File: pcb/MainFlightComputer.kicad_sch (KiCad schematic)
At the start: 73 parts, among them J1 614105150721, J3 Micro_SD_Card, J4 Pinout, J5 Debug, SW1 B3U-1000P-B, SW2 B3U-1000P-B, U1 STM32H533VET6, U2 MCP2221A-I/ST, U3 AP2112K-3.3

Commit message: Placed down most of the components.
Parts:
- removed JP4: SolderJumper_2_Open, Jumper:SolderJumper-2_P1.3mm_Open_RoundedPad1.0x1.5mm, symbol Jumper:SolderJumper_2_Open
- added R32: 100, Resistor_SMD:R_1206_3216Metric_Pad1.30x1.75mm_HandSolder, symbol Device:R
- SW1, SW2: value B3U-1000P-B -> B3U-1000P; footprint Button_Switch_SMD:SW_SPST_B3U-1000P-B -> Button_Switch_SMD:SW_SPST_B3U-1000P
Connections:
- net +3.3V: now also R32.1
- net RESET: now also R32.2
- net VBUS_VIN_LED_ANODE: now reaches D5.2 (A), R15.2
- net RESET_PRESSED: now reaches R16.1, SW1.2
- net BUTTON_PRESSED: now reaches R18.1, SW2.2
- net VBUS_VOUT_LED_ANODE: now reaches D3.2 (A), R14.2
- net BOOT0_VALUE: now reaches JP1.2 (C), R17.1
- net DEBUG_LED_G_CATHODE: now reaches D4.4 (GK), R12.1
- net DEBUG_LED_B_CATHODE: now reaches D4.2 (BK), R13.1
- net DEBUG_LED_R_CATHODE: now reaches D4.3 (RK), R11.1
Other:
- note added: "Debug LED (V2 : Added net-labels)."
- note added: "Reset Mechanism (V3 : Pull-up footprint)."
- note added: "USB-UART Bridge (V5 : Added more net-labels)."
- note removed: "Debug LED (V1 : Lowercase nets)."
- note removed: "Reset Mechanism."
- note removed: "USB-UART Bridge (V4 : Added net-labels)."
- moved on the sheet: C11, D3, D5, R11, R13, R16, R17, R18, SW1

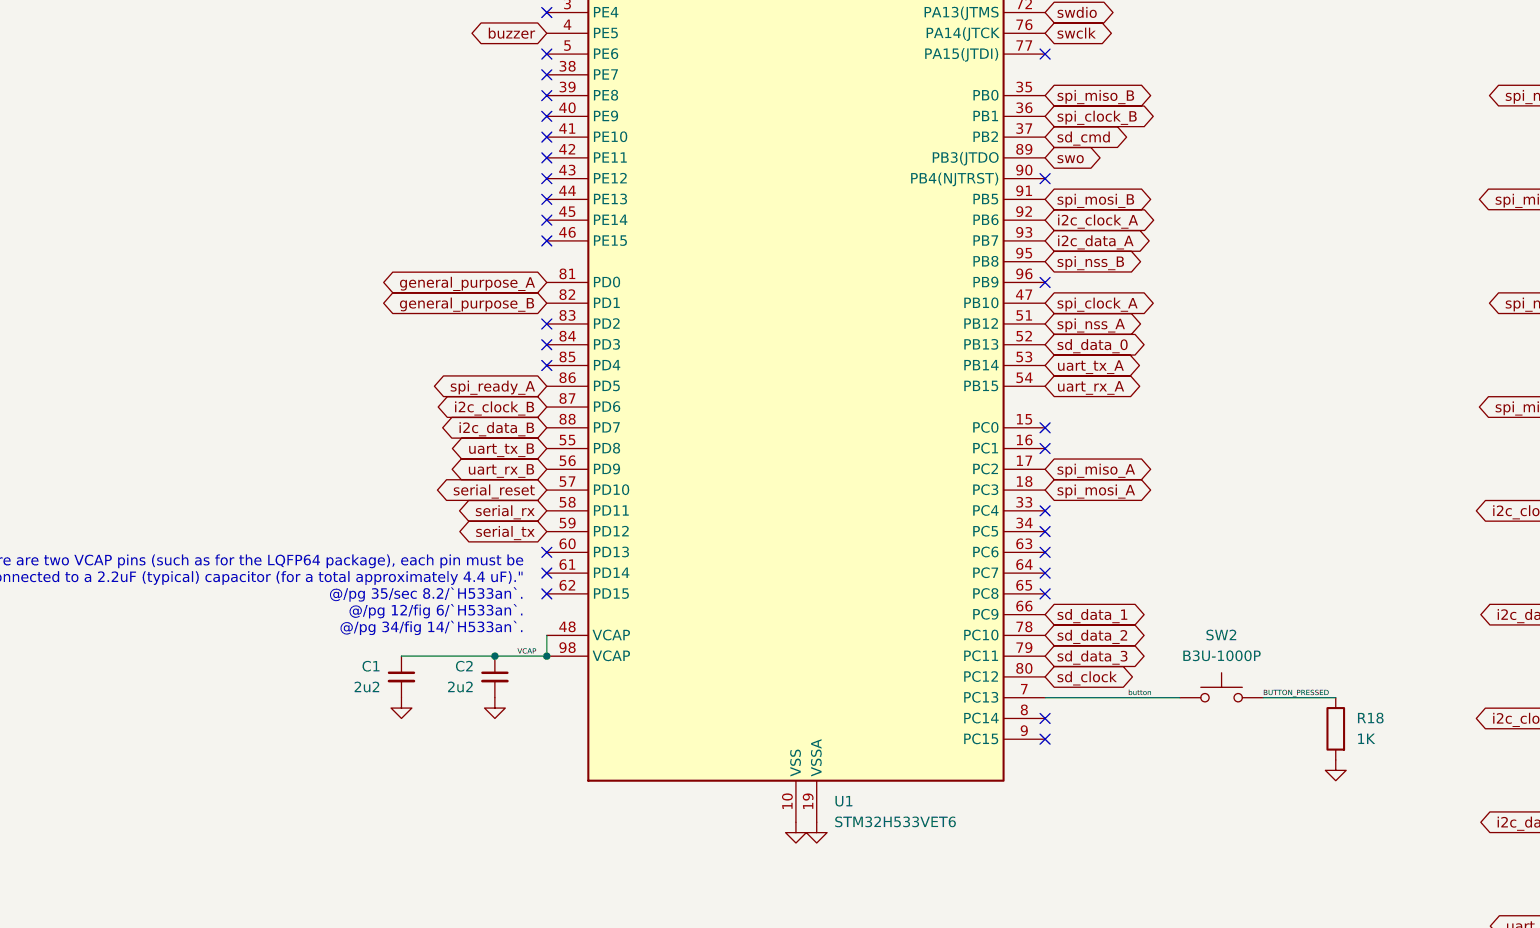
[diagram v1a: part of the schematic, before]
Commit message: Routed user button.
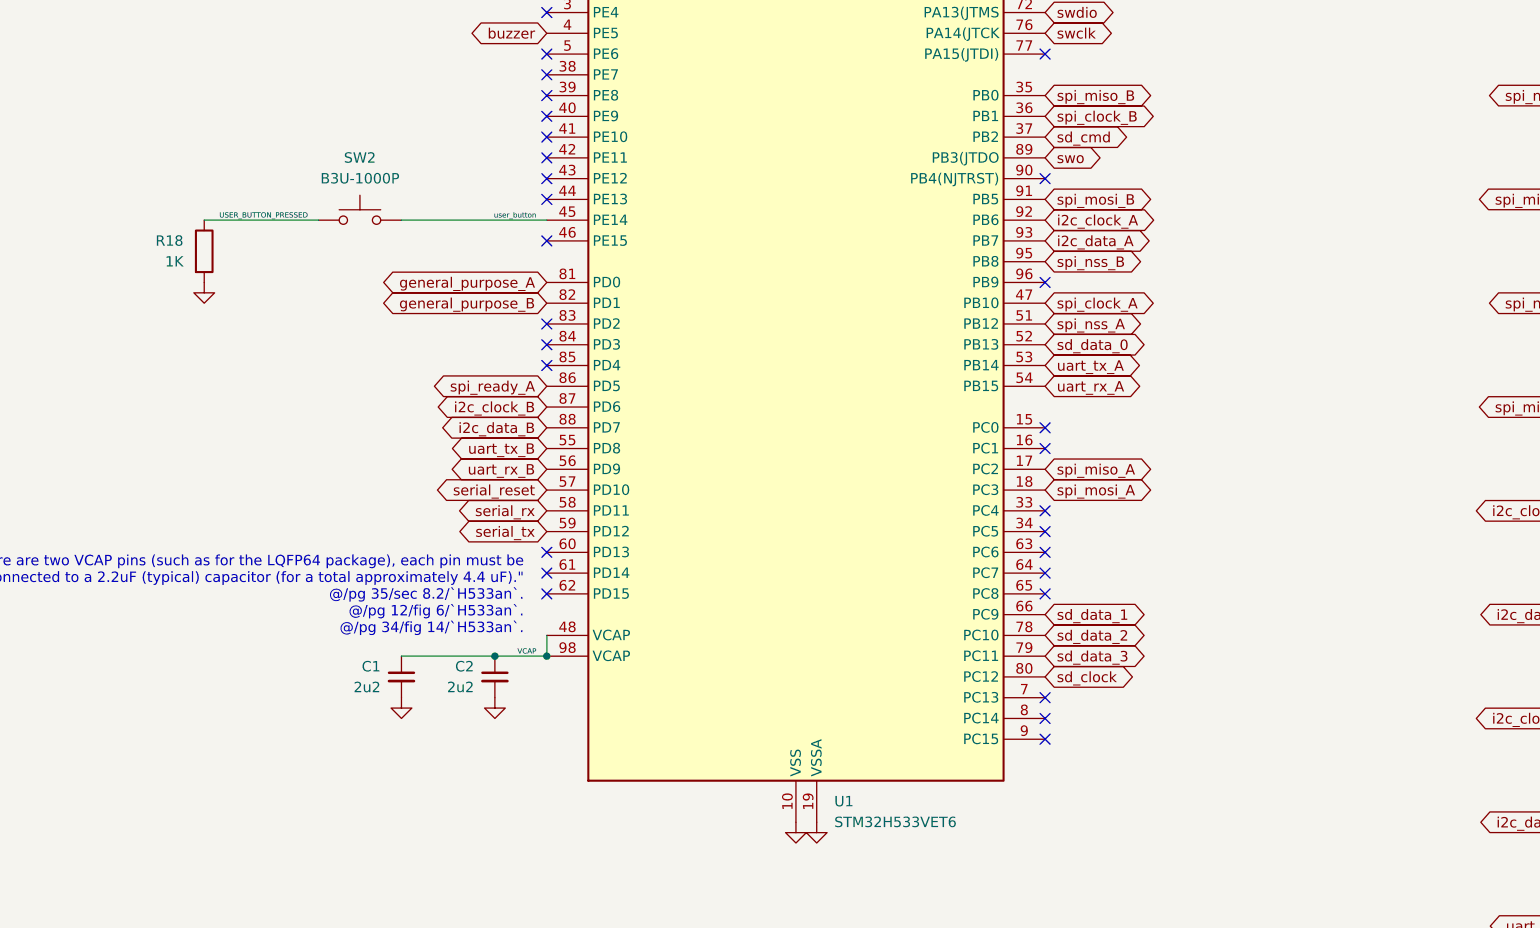
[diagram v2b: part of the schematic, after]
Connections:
- net user_button: now reaches U1.45 (PE14)
- net user_button: now also SW2.1
- net BUTTON_PRESSED renamed USER_BUTTON_PRESSED
- net button: no longer names the net of U1.7 (PC13)
- net button: no longer SW2.1
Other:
- moved on the sheet: R18, SW2

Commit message: Routed `led_channel_x`.
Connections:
- net led_channel_blue: now also U1.3 (PE4); no longer U1.31 (PA6)
- net led_channel_green: now also U1.2 (PE3); no longer U1.30 (PA5)
- net led_channel_red: now also U1.1 (PE2); no longer U1.29 (PA4)

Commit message: Routed uSD connector.
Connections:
- net sd_cmd: now also U1.83 (PD2); no longer U1.37 (PB2)
- net sd_data_0: now also U1.65 (PC8); no longer U1.52 (PB13)
- net SD_DAT2: now reaches J3.1 (DAT2), R1.2
- net SD_CLK: now reaches J3.5 (CLK), R2.2
- net SD_DAT3: now reaches J3.2 (DAT3/CD), R4.2
- net SD_DAT0: now reaches J3.7 (DAT0), R3.2
- net SD_CMD: now reaches J3.3 (CMD), R6.2
- net SD_DAT1: now reaches J3.8 (DAT1), R5.2
- no-connect marks 46 -> 45
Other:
- note added: "uSD Connector (V3 : Net-labels)."
- note removed: "uSD Connector (V2 : More verbose net-names)."
- moved on the sheet: J3, J5

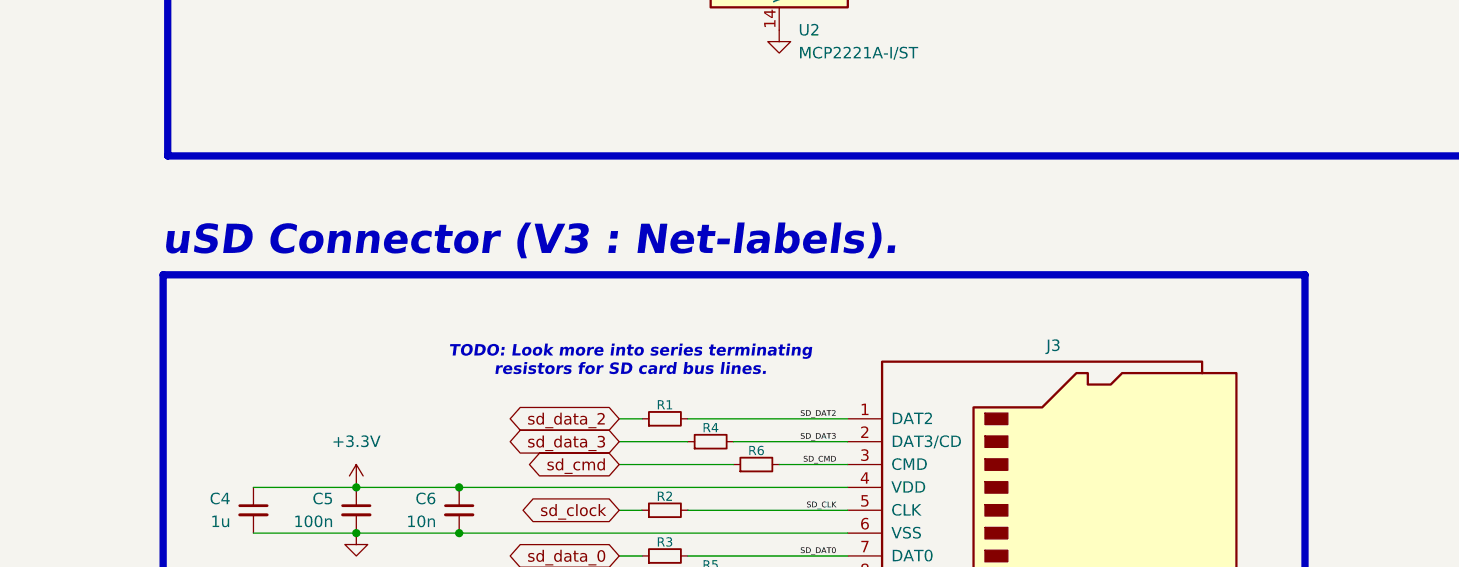
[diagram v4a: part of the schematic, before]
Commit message: Added part number to uSD connector.
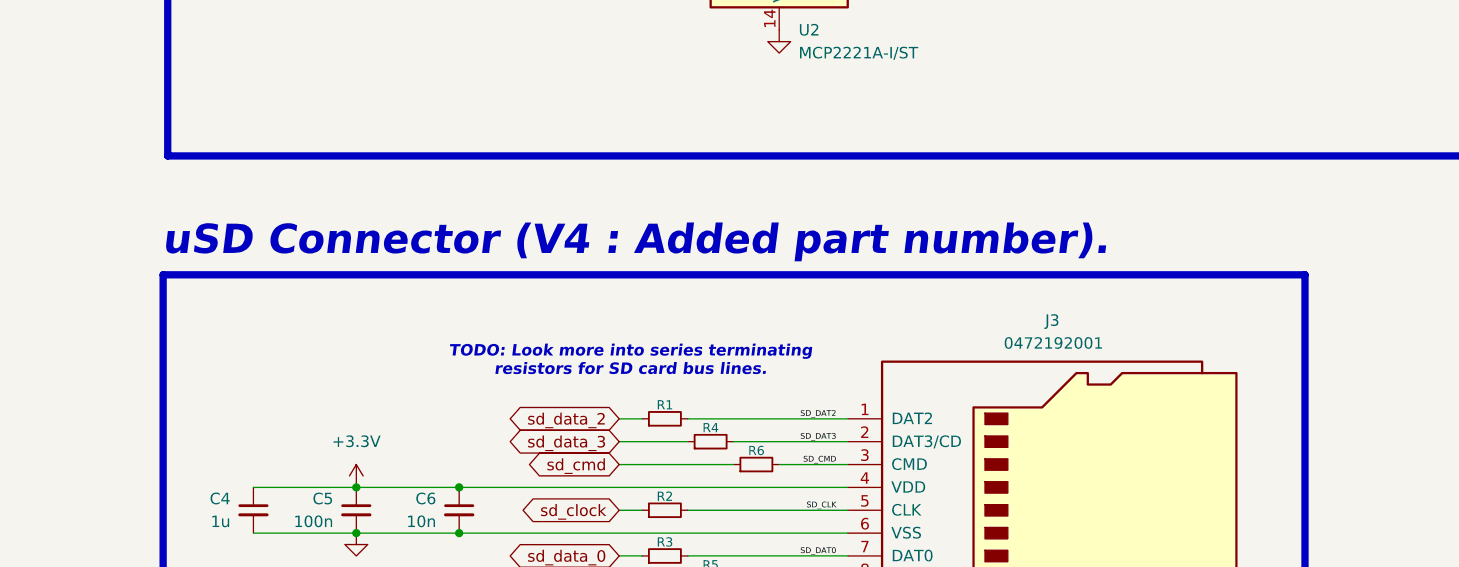
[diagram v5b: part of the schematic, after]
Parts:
- C10, C7, JP1, JP3, R1, R2, R3, R4, R5, R6: now in the parts list
- J3: value Micro_SD_Card -> 0472192001
- N1: now left out of the parts list
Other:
- note added: "uSD Connector (V4 : Added part number)."
- note removed: "uSD Connector (V3 : Net-labels)."

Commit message: Using vertical IDC header instead of horizontal because it's cheaper.
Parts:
- J4: footprint pcb:IDC-Header_2x17_P2.54mm_Horizontal -> pcb:IDC-Header_2x17_P2.54mm_Vertical

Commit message: Addressed ERC issues.
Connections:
- net SD_CLK renamed SD_CONNECTOR_CLK
- net SD_CMD renamed SD_CONNECTOR_CMD
- net SD_DAT0 renamed SD_CONNECTOR_DAT0
- net SD_DAT1 renamed SD_CONNECTOR_DAT1
- net SD_DAT2 renamed SD_CONNECTOR_DAT2
- net SD_DAT3 renamed SD_CONNECTOR_DAT3
- no-connect marks 45 -> 46
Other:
- note added: "uSD Connector (V5 : Addressed ERC)."
- note removed: "uSD Connector (V4 : Added part number)."
- moved on the sheet: J3

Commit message: changed resistor values for LED
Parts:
- R11: value 2K -> 300
- R12, R13: value 2K -> 100
